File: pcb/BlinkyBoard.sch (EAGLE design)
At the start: 25 parts, among them Q1 16 MHz

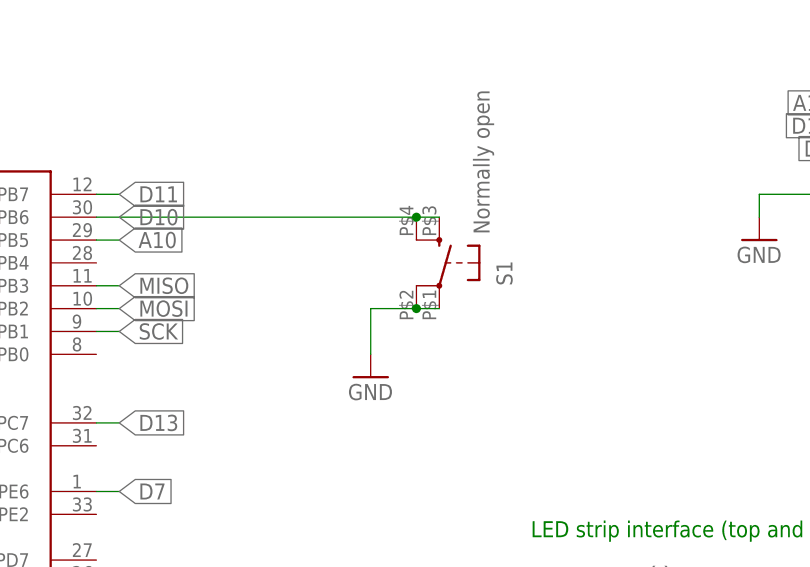
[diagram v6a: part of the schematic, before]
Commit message: Flip gnd/5v to match WS2812B strip.
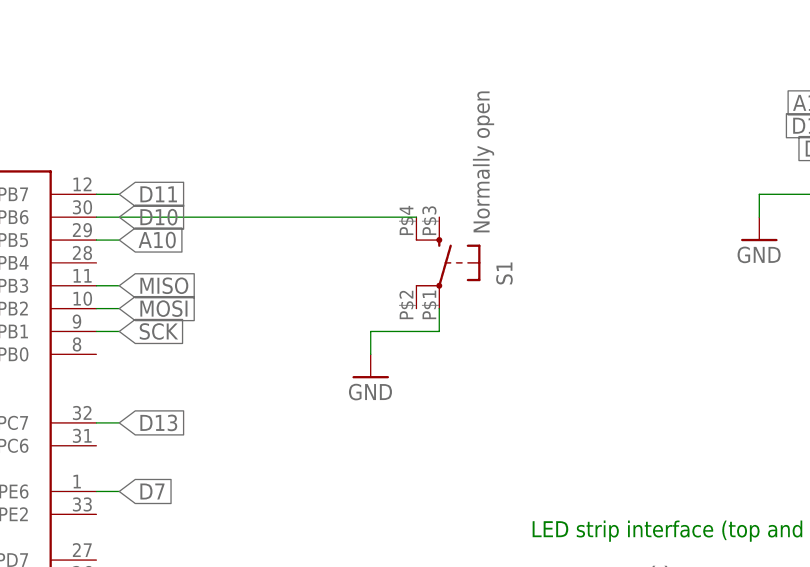
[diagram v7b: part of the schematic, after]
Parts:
- S1: device blinkyboard:GLOWBOARD_KMR211G -> blinkiverse:GLOWBOARD_KMR211G
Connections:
- net D10: no longer S1.S
- net GND: no longer S1.P1
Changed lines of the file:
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@@
 <?xml version="1.0" encoding="utf-8"?>
 <!DOCTYPE eagle SYSTEM "eagle.dtd">
-<eagle version="6.4">
+<eagle version="6.5.0">
 <drawing>
 <settings>
@@
 <part name="P+6" library="supply1" deviceset="VCC" device=""/>
 <part name="P+7" library="supply1" deviceset="VCC" device=""/>
-<part name="S1" library="blinkyboard" deviceset="GLOWBOARD_KMR211G" device="" value="Normally open"/>
+<part name="S1" library="blinkiverse" deviceset="GLOWBOARD_KMR211G" device="" value="Normally open"/>
 <part name="Q1" library="blinkiverse" deviceset="CRYSTAL_4PAD" device="2520" value="16 MHz"/>
 <part name="C4" library="blinkiverse" deviceset="C_US" device="" value="0.1uF"/>
@@
 </segment>
 <segment>
-<wire x1="127" y1="68.58" x2="127" y2="73.66" width="0.1524" layer="91"/>
+<wire x1="127" y1="68.58" x2="127" y2="71.12" width="0.1524" layer="91"/>
 <pinref part="GND7" gate="1" pin="GND"/>
 <pinref part="S1" gate="1" pin="P"/>
-<pinref part="S1" gate="1" pin="P1"/>
-<wire x1="134.62" y1="73.66" x2="132.08" y2="73.66" width="0.1524" layer="91"/>
-<wire x1="132.08" y1="73.66" x2="127" y2="73.66" width="0.1524" layer="91"/>
-<junction x="132.08" y="73.66"/>
+<wire x1="134.62" y1="73.66" x2="134.62" y2="71.12" width="0.1524" layer="91"/>
+<wire x1="134.62" y1="71.12" x2="127" y2="71.12" width="0.1524" layer="91"/>
 </segment>
 <segment>
@@
 <segment>
 <pinref part="S1" gate="1" pin="S1"/>
-<pinref part="S1" gate="1" pin="S"/>
-<wire x1="134.62" y1="83.82" x2="132.08" y2="83.82" width="0.1524" layer="91"/>
 <pinref part="U$2" gate="G$1" pin="(PCINT6/OC1B/OC4B/ADC13)PB6"/>
 <wire x1="96.52" y1="83.82" x2="132.08" y2="83.82" width="0.1524" layer="91"/>
-<junction x="132.08" y="83.82"/>
 <label x="99.06" y="83.82" size="1.778" layer="95" xref="yes"/>
 </segment>

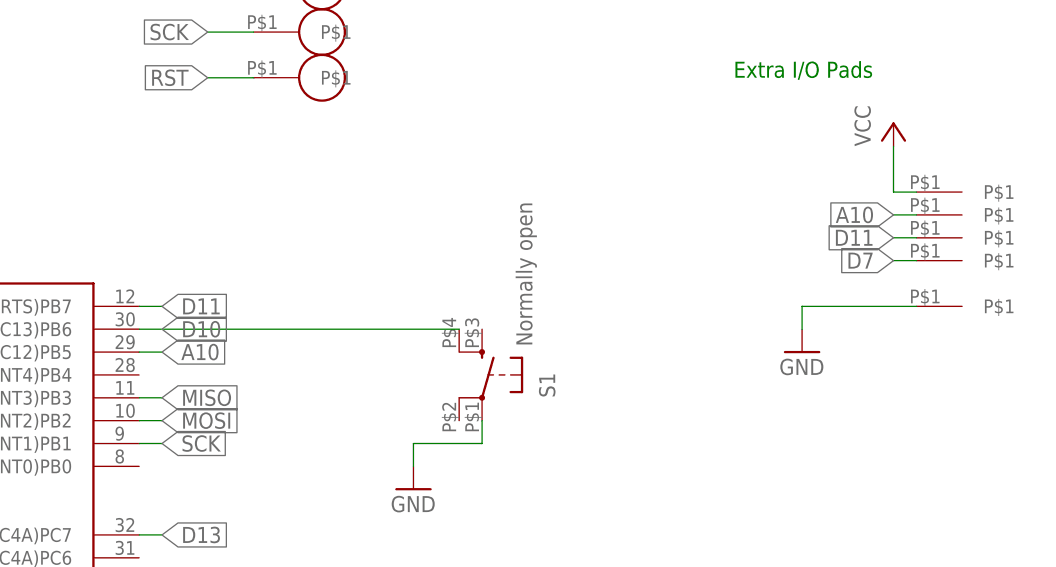
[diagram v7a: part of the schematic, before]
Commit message: Silkscreen fix: Analog is on A9, not A11!
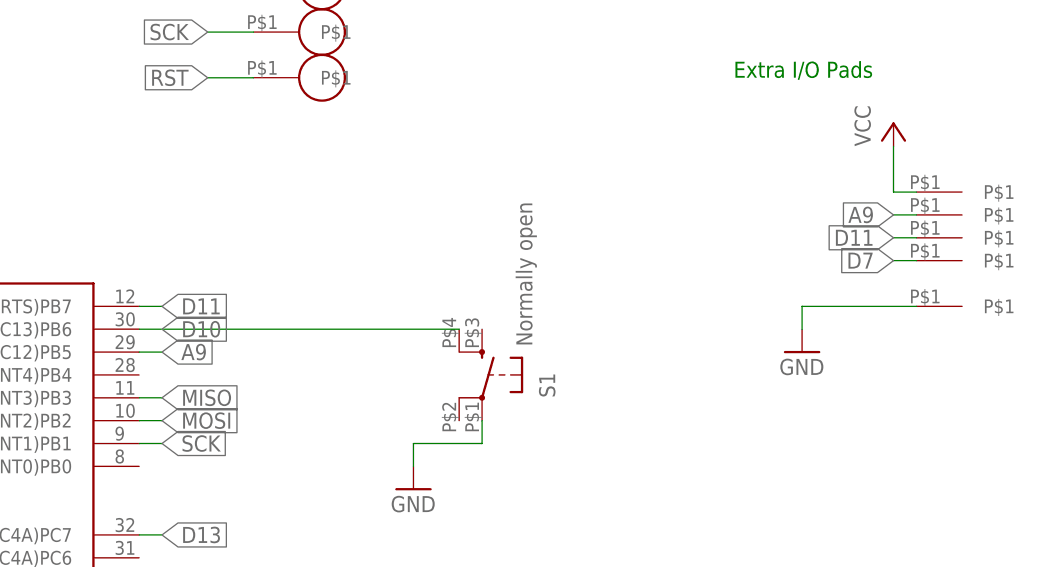
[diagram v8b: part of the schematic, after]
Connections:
- net A10 renamed A9
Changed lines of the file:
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@@
 <?xml version="1.0" encoding="utf-8"?>
 <!DOCTYPE eagle SYSTEM "eagle.dtd">
-<eagle version="6.5.0">
+<eagle version="6.4">
 <drawing>
 <settings>
@@
 </segment>
 </net>
-<net name="A10" class="0">
+<net name="A9" class="0">
 <segment>
 <pinref part="U$2" gate="G$1" pin="(PCINT5/OC1A/#OC4B/ADC12)PB5"/>
